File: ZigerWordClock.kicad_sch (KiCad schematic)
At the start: 21 parts, among them U1 BH1750, U10 BTF-5V-060L-B_SK9822_LED_Stri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, U11 BTF-5V-060L-B_SK9822_LED_Stri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, U12 BTF-5V-060L-B_SK9822_LED_Stri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, U13 BTF-5V-060L-B_SK9822_LED_Stri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, U14 BTF-5V-060L-B_SK9822_LED_Stri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, U15 BTF-5V-060L-B_SK9822_LED_Stri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, U16 BTF-5V-060L-B_SK9822_LED_Stri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, U17 BTF-5V-060L-B_SK9822_LED_Stri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, U18 BTF-5V-060L-B_SK9822_LED_Stri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, U19 BTF-5V-060L-B_SK9822_LED_Stri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, U2 LILYGO(R)_TTGO_T8_ESP32-S2_V1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, U3 BTF-5V-060L-B_SK9822_LED_Stri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, U4 LevelShifter, U5 BTF-5V-060L-B_SK9822_LED_Stri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, U6 BTF-5V-060L-B_SK9822_LED_Stri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, U7 BTF-5V-060L-B_SK9822_LED_Stri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, U8 BTF-5V-060L-B_SK9822_LED_Stri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, U9 BTF-5V-060L-B_SK9822_LED_Stri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

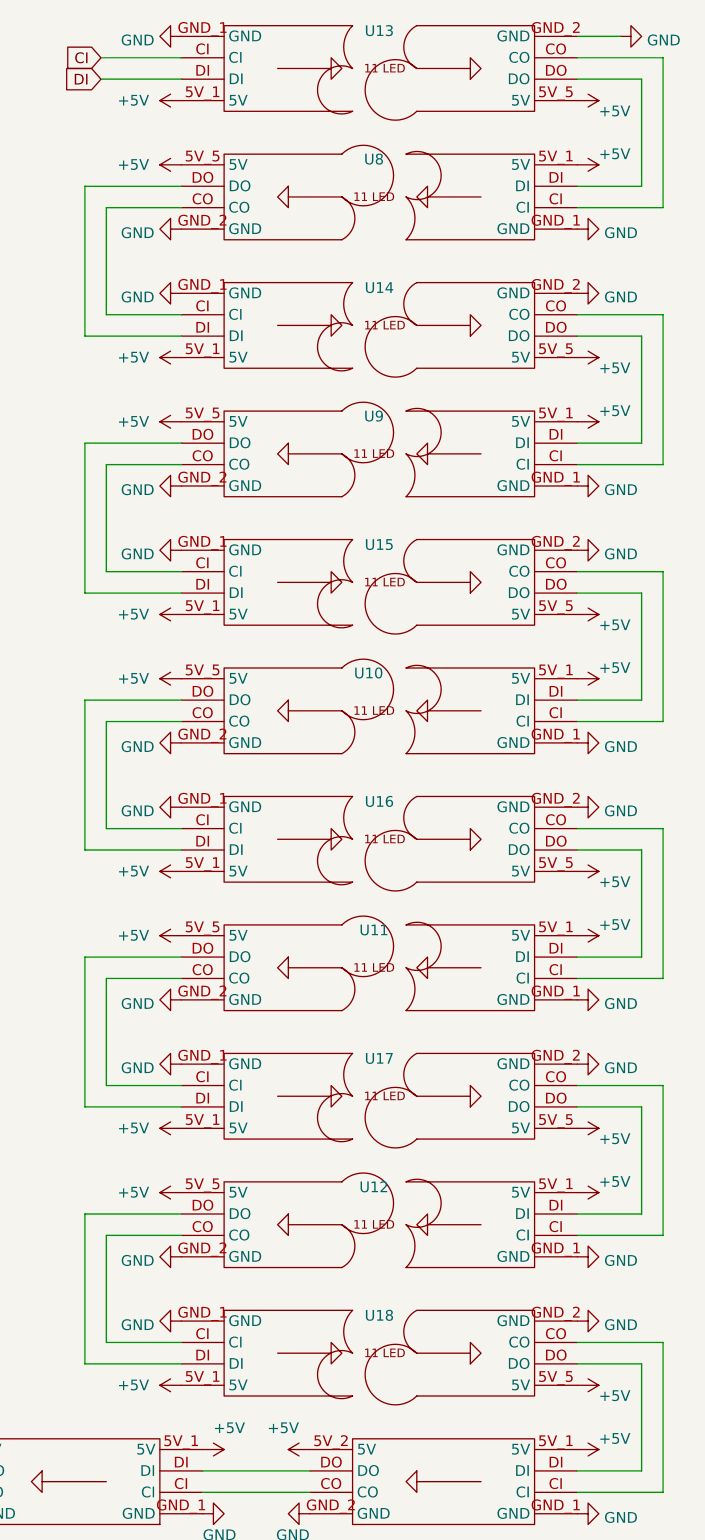
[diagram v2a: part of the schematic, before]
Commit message: Fixed library and missing footprints for i2c resistors
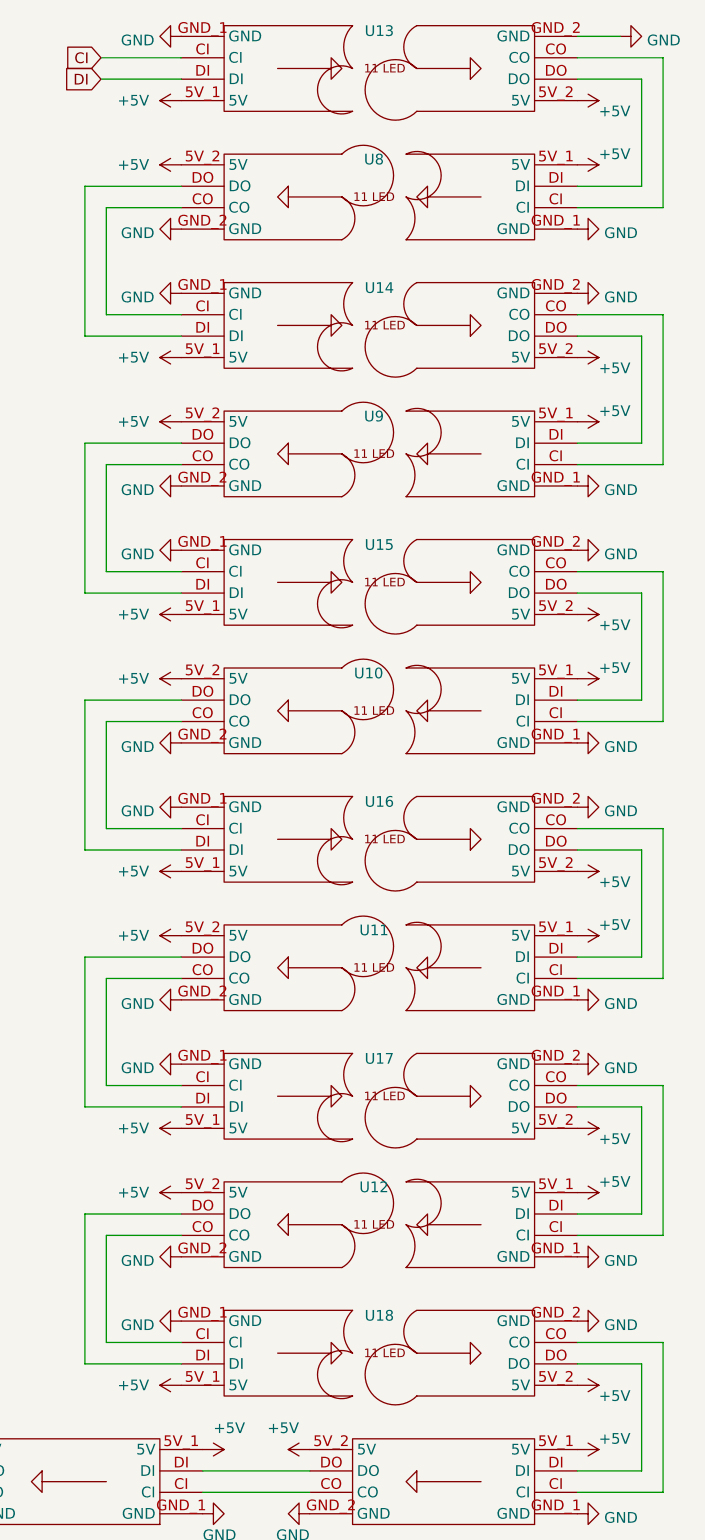
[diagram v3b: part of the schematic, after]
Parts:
- R1, R2: footprint (none) -> Resistor_THT:R_Axial_DIN0207_L6.3mm_D2.5mm_P10.16mm_Horizontal
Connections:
- net +5V: now also U10.5V_2 (5V), U11.5V_2 (5V), U12.5V_2 (5V), U13.5V_2 (5V), U14.5V_2 (5V), U15.5V_2 (5V), U16.5V_2 (5V), U17.5V_2 (5V), U18.5V_2 (5V), U8.5V_2 (5V), U9.5V_2 (5V); no longer U10.5V_5 (5V), U11.5V_5 (5V), U12.5V_5 (5V), U13.5V_5 (5V), U14.5V_5 (5V), U15.5V_5 (5V), U16.5V_5 (5V), U17.5V_5 (5V), U18.5V_5 (5V), U8.5V_5 (5V), U9.5V_5 (5V)

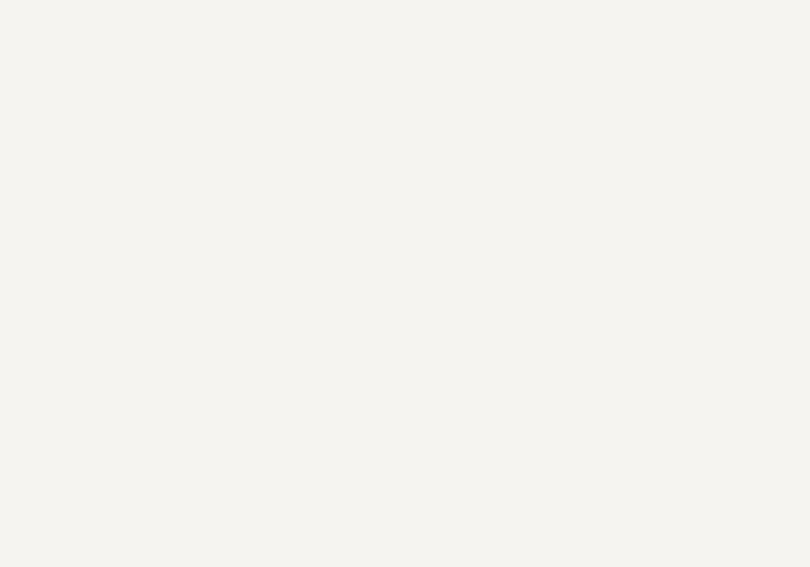
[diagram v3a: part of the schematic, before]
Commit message: Adds ir receiver to schematic and board
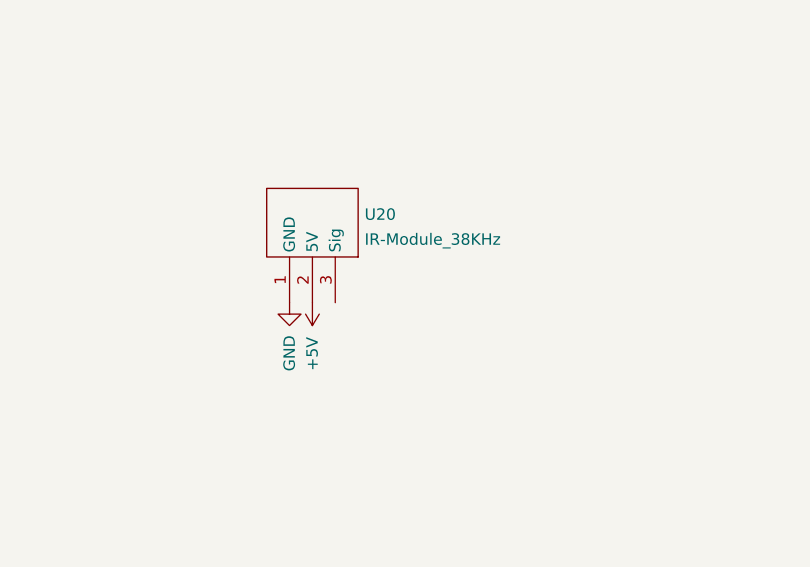
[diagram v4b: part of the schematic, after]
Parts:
- added U20: IR-Module_38KHz, WordClock Footprint Library:IR-Module_38KHz, symbol WordClock Symbol Library:IR-Module_38KHz
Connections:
- net +5V: now also U20.2 (5V)
- net GND: now also U20.1 (GND)
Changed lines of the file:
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@@
+    (pin "1")
+  )
+  (symbol (lib_id "power:GND") (at 222.25 72.39 0) (unit 1)
+    (in_bom yes) (on_board yes)
+    (property "Reference" "#PWR?" (id 0) (at 222.25 78.74 0)
+      (effects (font (size 1.27 1.27)) hide)
+    )
+    (property "Value" "GND" (id 1) (at 222.25 80.01 90)
+      (effects (font (size 1.27 1.27)) (justify left))
+    )
+    (property "Footprint" "" (id 2) (at 222.25 72.39 0)
+      (effects (font (size 1.27 1.27)) hide)
+    )
+    (property "Datasheet" "" (id 3) (at 222.25 72.39 0)
+      (effects (font (size 1.27 1.27)) hide)
+    )
     (pin "1")
   )
@@
     (pin "1")
   )
+  (symbol (lib_id "power:+5V") (at 224.79 72.39 0) (mirror x) (unit 1)
+    (in_bom yes) (on_board yes)
+    (property "Reference" "#PWR?" (id 0) (at 224.79 68.58 0)
+      (effects (font (size 1.27 1.27)) hide)
+    )
+    (property "Value" "+5V" (id 1) (at 224.79 76.2 90)
+      (effects (font (size 1.27 1.27)) (justify left))
+    )
+    (property "Footprint" "" (id 2) (at 224.79 72.39 0)
+      (effects (font (size 1.27 1.27)) hide)
+    )
+    (property "Datasheet" "" (id 3) (at 224.79 72.39 0)
+      (effects (font (size 1.27 1.27)) hide)
+    )
+    (pin "1")
+  )
   (symbol (lib_id "WordClock Symbol Library:BTF-5V-060L-B_SK9822_LED_Strip_-_1_LED") (at 228.6 213.36 180) (unit 1)
     (in_bom yes) (on_board yes)
@@
     (pin "1")
   )
+  (symbol (lib_id "WordClock Symbol Library:IR-Module_38KHz") (at 224.79 60.96 0) (unit 1)
+    (in_bom yes) (on_board yes) (fields_autoplaced)
+    (property "Reference" "U20" (id 0) (at 230.5812 62.5915 0)
+      (effects (font (size 1.27 1.27)) (justify left))
+    )
+    (property "Value" "IR-Module_38KHz" (id 1) (at 230.5812 65.3666 0)
+      (effects (font (size 1.27 1.27)) (justify left))
+    )
+    (property "Footprint" "WordClock Footprint Library:IR-Module_38KHz" (id 2) (at 224.79 60.96 0)
+      (effects (font (size 1.27 1.27)) hide)
+    )
+    (property "Datasheet" "" (id 3) (at 224.79 60.96 0)
+      (effects (font (size 1.27 1.27)) hide)
+    )
+    (pin "1")
+    (pin "2")
+    (pin "3")
+  )
   (symbol (lib_id "power:+5V") (at 378.46 195.58 270) (unit 1)
     (in_bom yes) (on_board yes)
@@
       (reference "#PWR0172") (unit 1) (value "+5V") (footprint "")
     )
+    (path "/294577b6-86d9-48bd-b62d-99f36b18bc9e"
+      (reference "#PWR?") (unit 1) (value "GND") (footprint "")
+    )
+    (path "/b5952712-de20-4c56-a4c0-1e21105f1102"
+      (reference "#PWR?") (unit 1) (value "+5V") (footprint "")
+    )
     (path "/18816637-ac20-4b13-9b79-5c791d4645f8"
       (reference "R1") (unit 1) (value "R") (footprint "Resistor_THT:R_Axial_DIN0207_L6.3mm_D2.5mm_P10.16mm_Horizontal")
@@
       (reference "U19") (unit 1) (value "BTF-5V-060L-B_SK9822_LED_Strip_-_1_LED") (footprint "WordClock Footprint Library:BTF-5V-060L-B SK9822 LED Strip - 1 Segment")
     )
-  )
+    (path "/d243a351-1076-404d-87d3-ffbe6c05b4ad"
+      (reference "U20") (unit 1) (value "IR-Module_38KHz") (footprint "WordClock Footprint Library:IR-Module_38KHz")
+    )
+  )

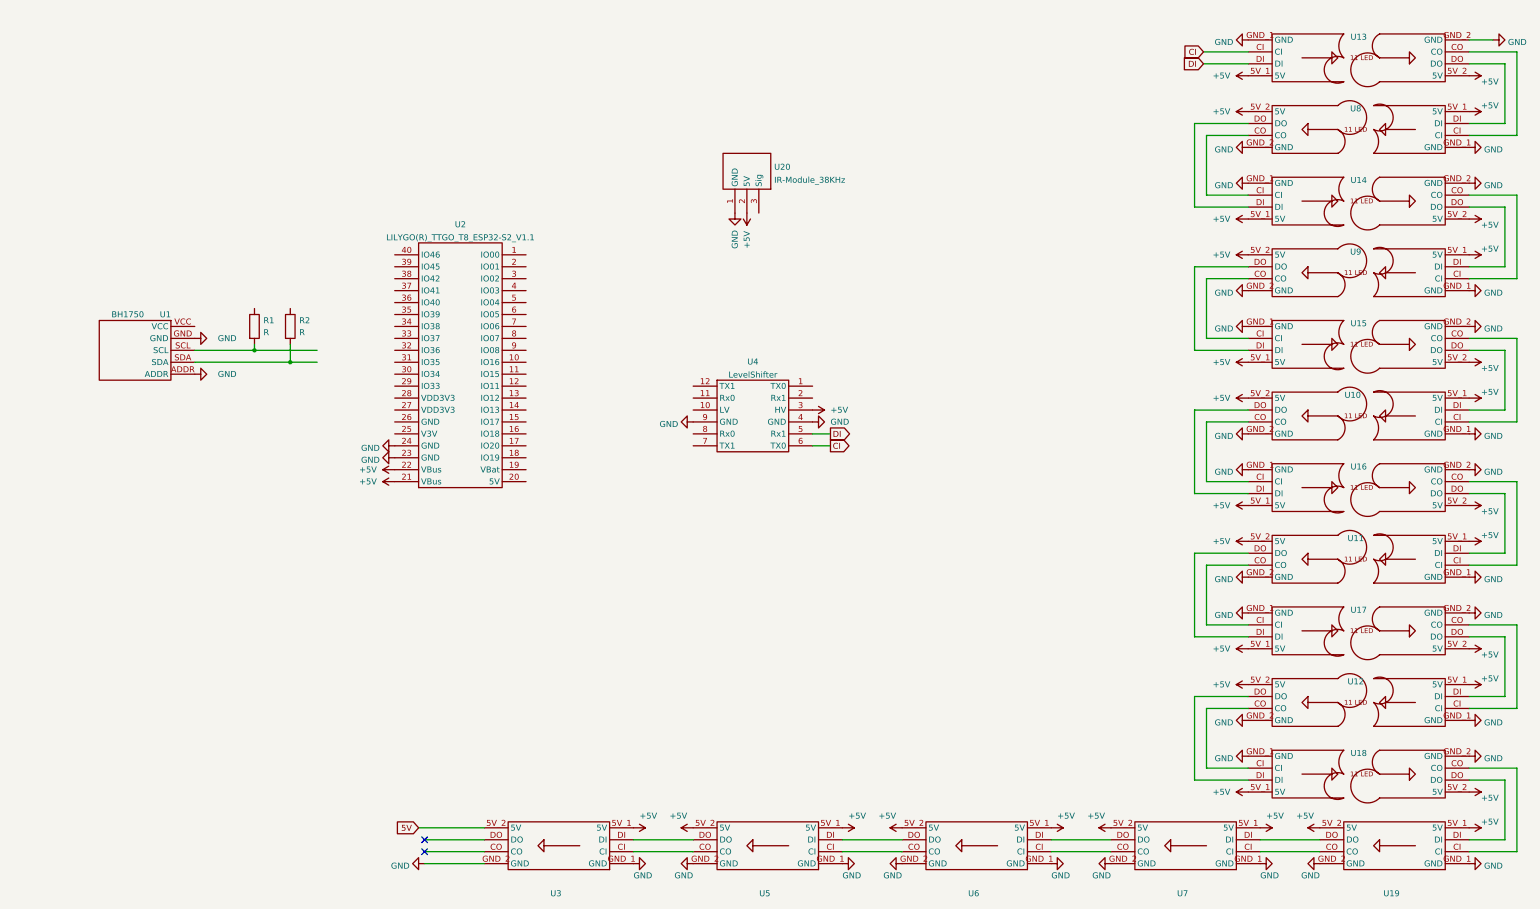
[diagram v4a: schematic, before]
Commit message: Added some connections
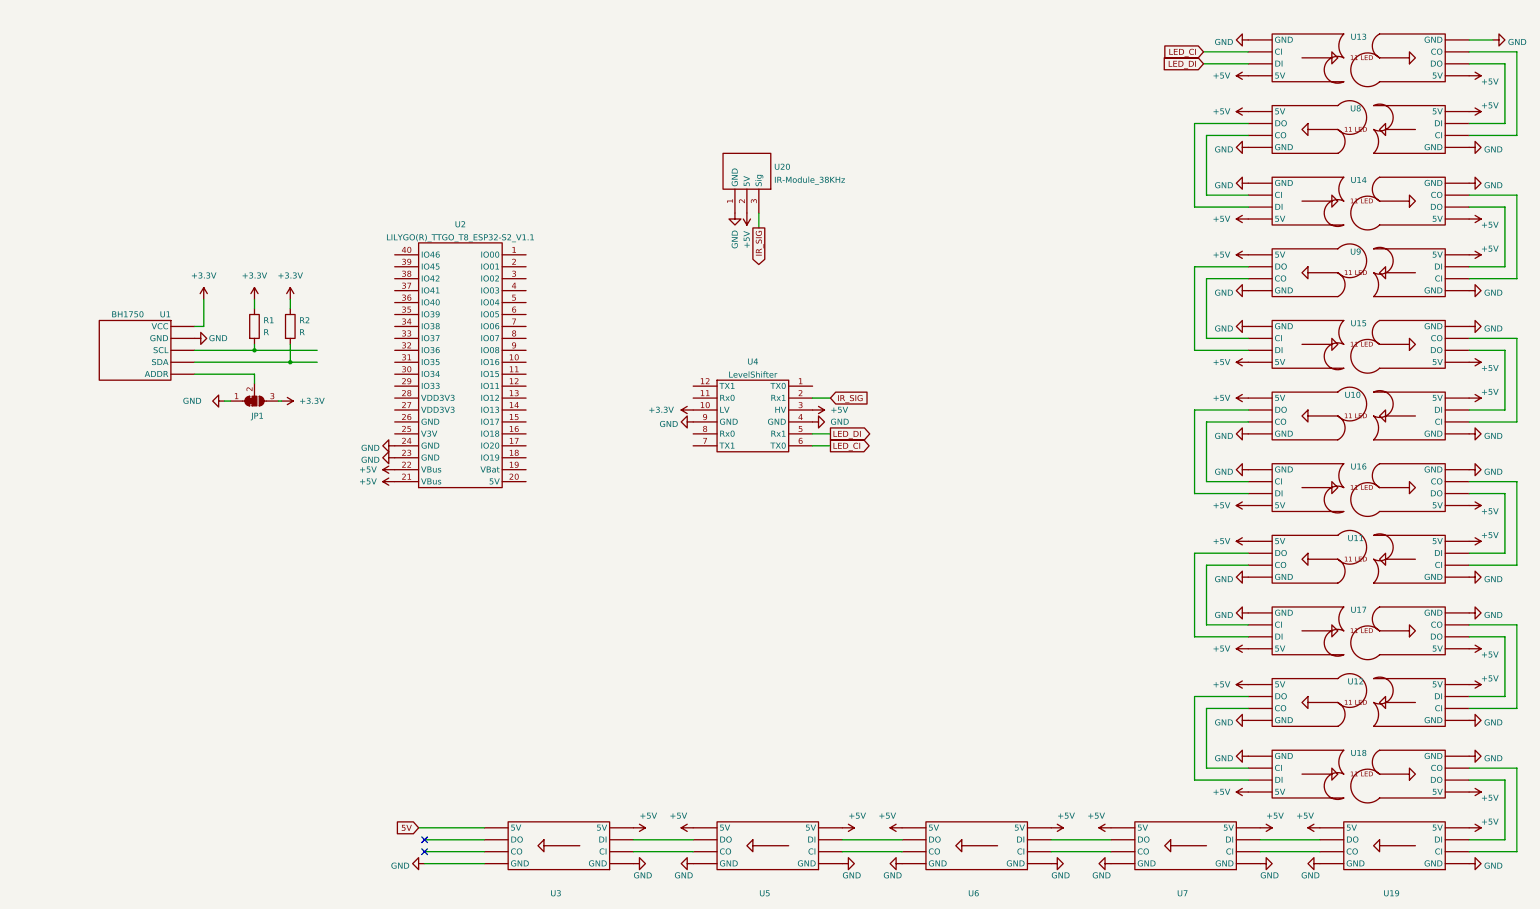
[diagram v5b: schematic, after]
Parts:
- added JP1: SolderJumper_3_Bridged12, Jumper:SolderJumper-3_P1.3mm_Bridged12_RoundedPad1.0x1.5mm_NumberLabels, symbol Jumper:SolderJumper_3_Bridged12
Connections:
- net GND: now also JP1.1 (A); no longer U1.ADDR
- net +3V3: now reaches R1.1
- net +3V3: now also R2.1, U1.VCC, U4.10 (LV), JP1.3 (B)
- net IR_SIG: now reaches U4.2 (Rx1)
- net IR_SIG: now also U20.3 (Sig)
- net CI renamed LED_CI
- net DI renamed LED_DI
- new net: JP1.2 (C), U1.ADDR

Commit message: finalized pins, fixed ESP libs
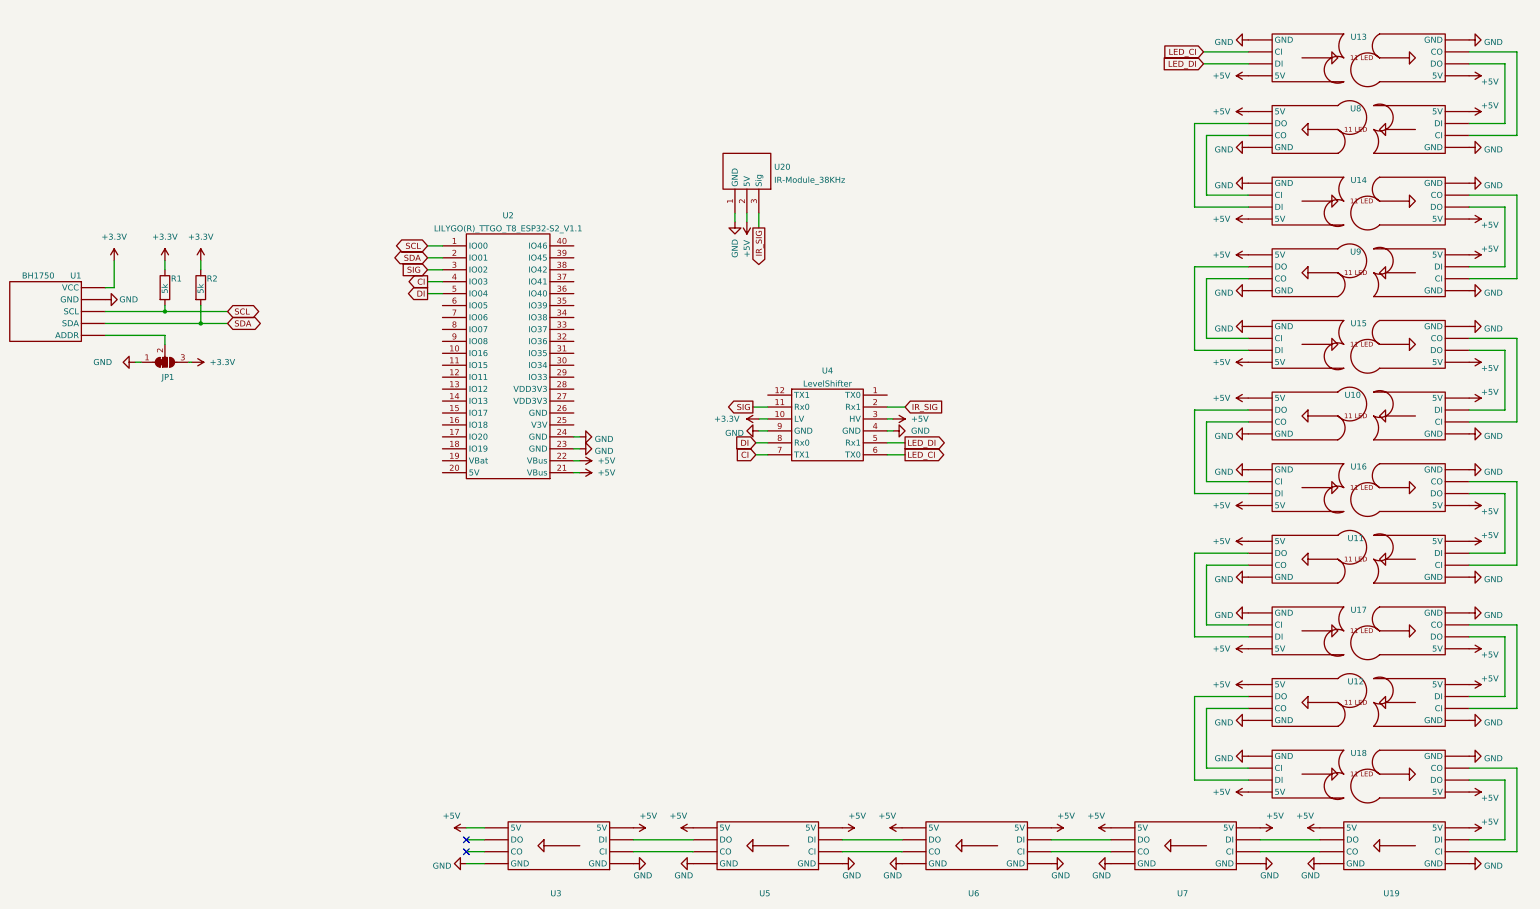
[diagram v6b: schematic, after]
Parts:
- R1, R2: value R -> 5k
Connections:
- net 5V is gone; now on net +5V: U3.5V_2 (5V)
- net SCL: now reaches R1.2, U1.SCL
- net SCL: now also U2.1 (IO00)
- net SIG: now reaches U4.11 (Rx0)
- net SIG: now also U2.3 (IO02)
- net CI: now reaches U4.7 (TX1)
- net CI: now also U2.4 (IO03)
- net DI: now reaches U4.8 (Rx0)
- net DI: now also U2.5 (IO04)
- net SDA: now reaches U2.2 (IO01)
- net SDA: now also R2.2, U1.SDA
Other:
- moved on the sheet: JP1, R1, R2, U1, U2, U4

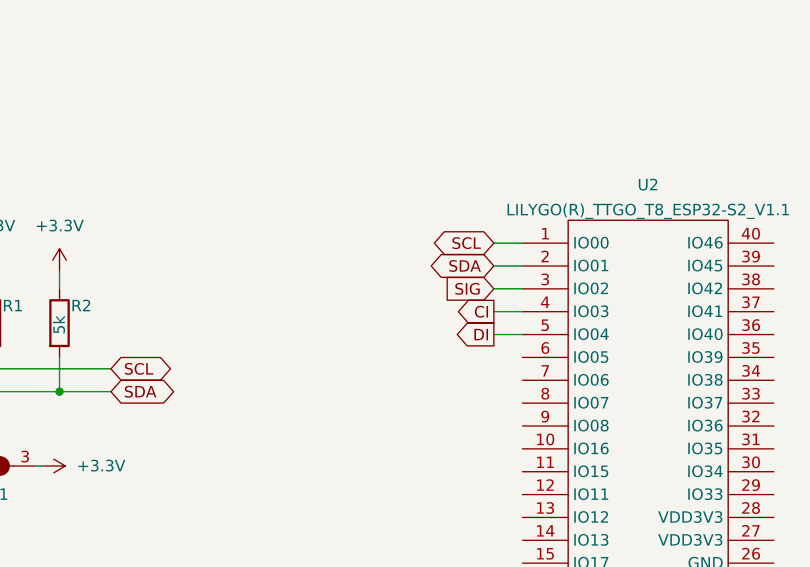
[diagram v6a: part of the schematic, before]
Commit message: pads added to libs
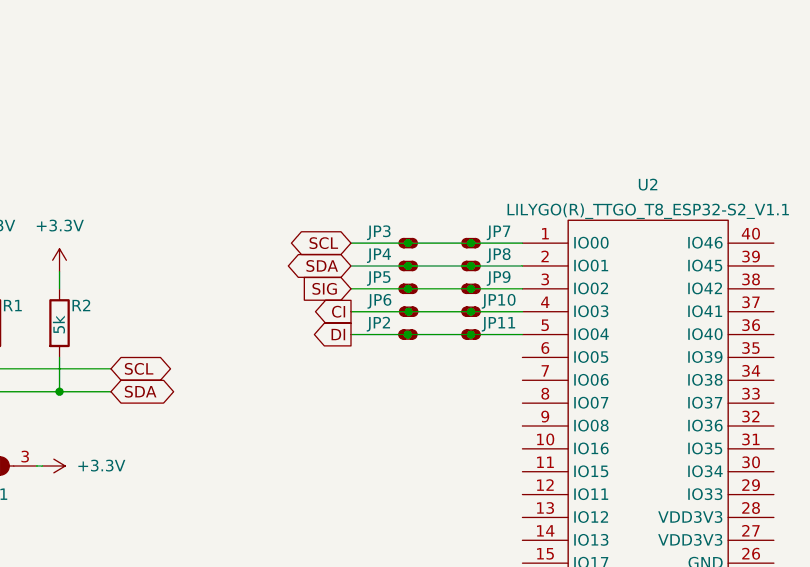
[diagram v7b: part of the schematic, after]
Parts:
- added JP10, JP11, JP2, JP3, JP4, JP5, JP6, JP7, JP8, JP9: Pad, WordClock Footprint Library:Pad, symbol WordClock Symbol Library:Pad
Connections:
- net CI: now also JP10.1, JP6.1
- net DI: now also JP11.1, JP2.1
- net SCL: now also JP3.1, JP7.1
- net SDA: now also JP4.1, JP8.1
- net SIG: now also JP5.1, JP9.1
